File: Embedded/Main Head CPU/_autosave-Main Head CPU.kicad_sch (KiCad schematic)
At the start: 47 parts, among them J1 10171746-00021LF, J10 Fan 1, J11 Substructure Power, J12 Head Power, J13 MicroSD, J2 Maw, J3 Tongue, J4 Left Fin, J5 Right Fin, J6 Scales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

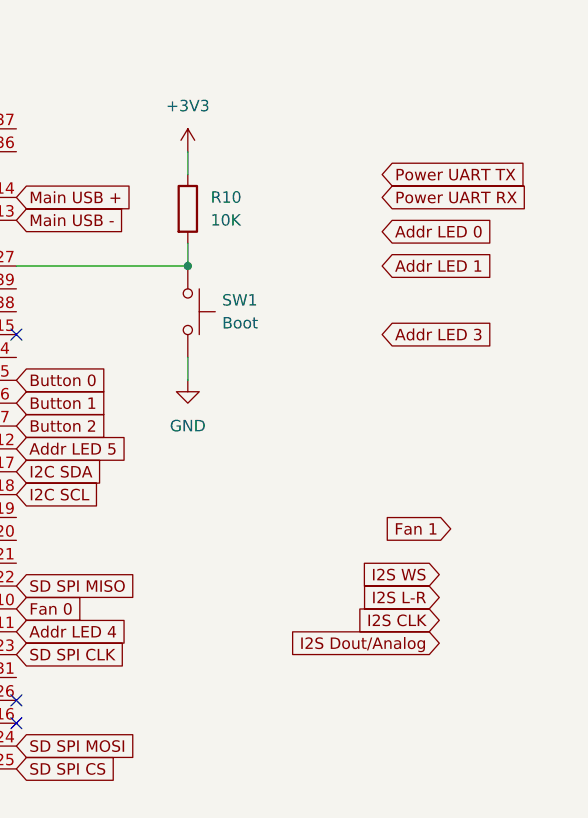
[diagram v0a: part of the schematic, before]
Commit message: Added Routing for majority of signals
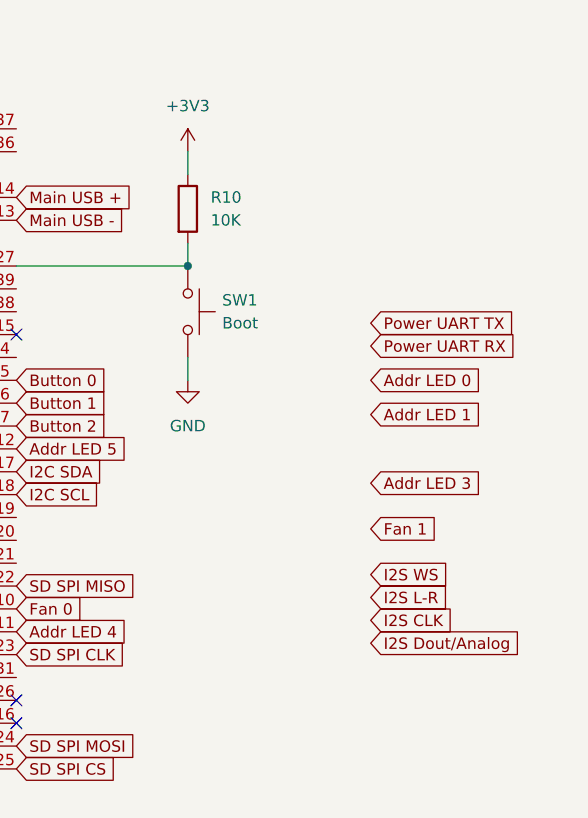
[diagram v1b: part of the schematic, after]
